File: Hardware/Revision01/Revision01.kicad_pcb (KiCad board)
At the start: 4 copper layers, 100 x 119.8 mm, 96 parts, among them J1 Battery connector, J11 RGBW connector, J2 StrainConn, J3 StrainConn, J4 StrainConn, J5 StrainConn, J6 StrainConn, J7 StrainConn, J8 StrainConn, J9 StrainConn, Q1 PMOS, Q2 NMOS, Q3 PMOS, SW1 StartStop_Push, SW2 ON/OFF_SW_SPST_LED, U1 NCP1117LPST50T3G, U2 NUCLEO-L476RG, U3 LP5813BDRRR, U4 MRF89XAM9AT-I/RM, U5 ICM-45605

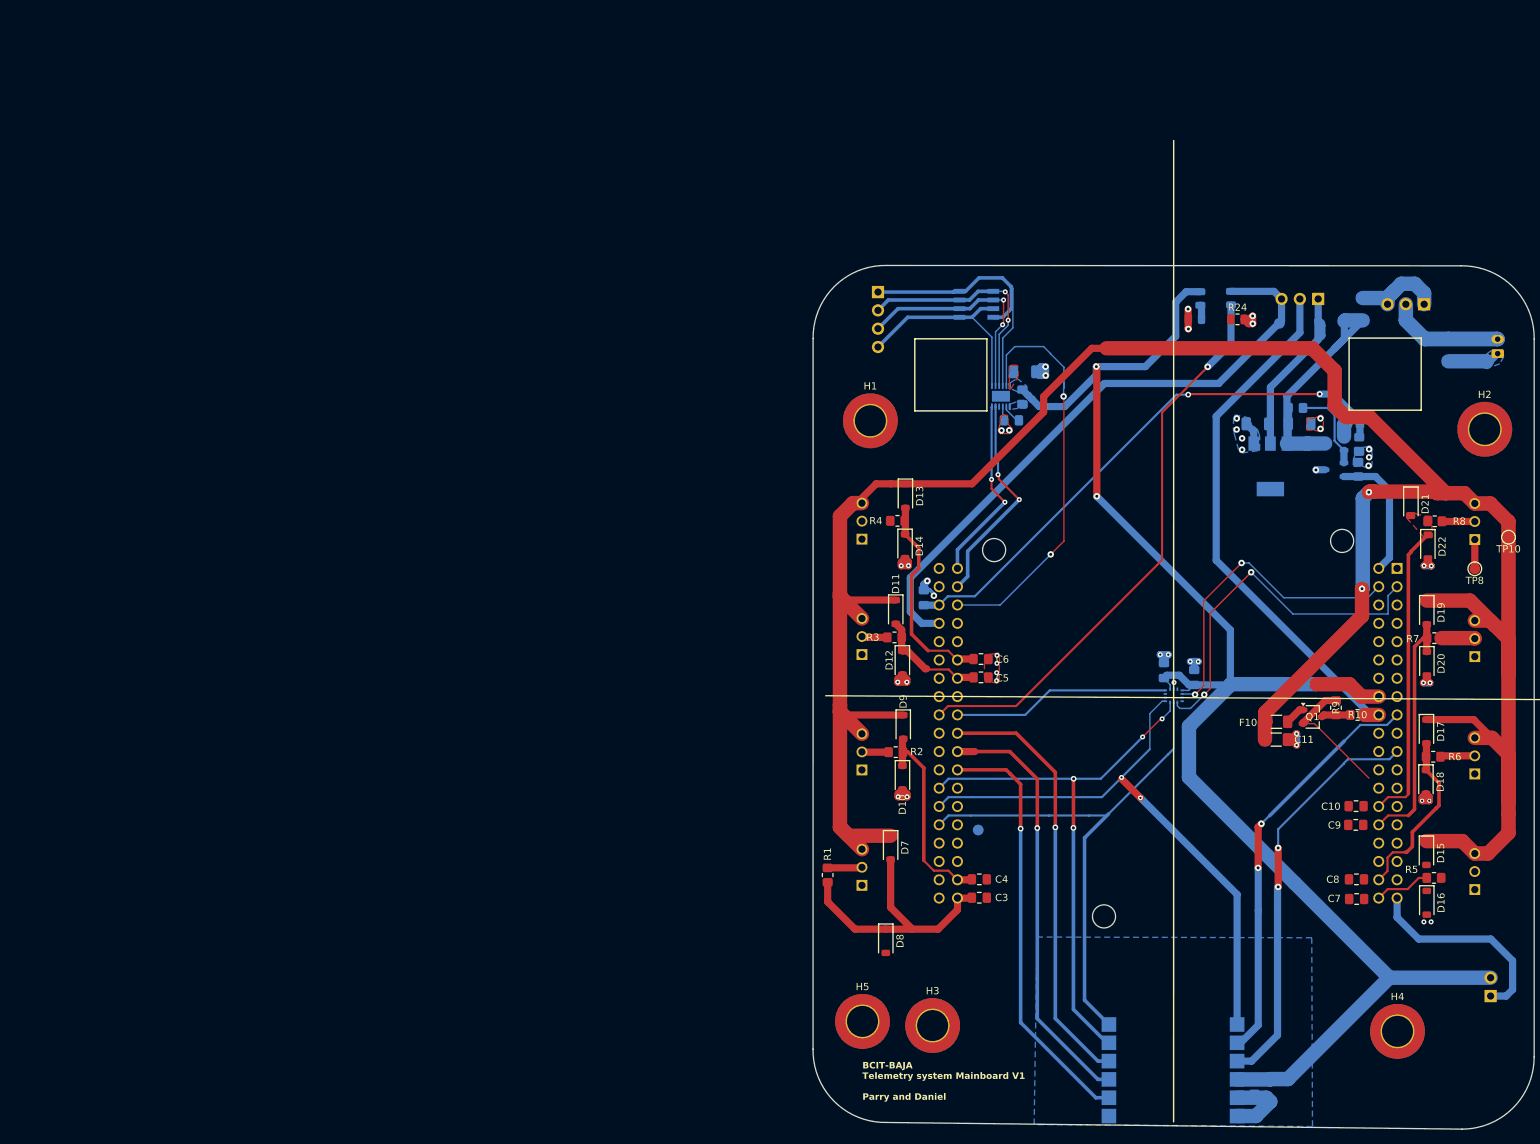
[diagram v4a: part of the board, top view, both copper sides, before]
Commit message: rewired and re-routed traces on strainAmplifier
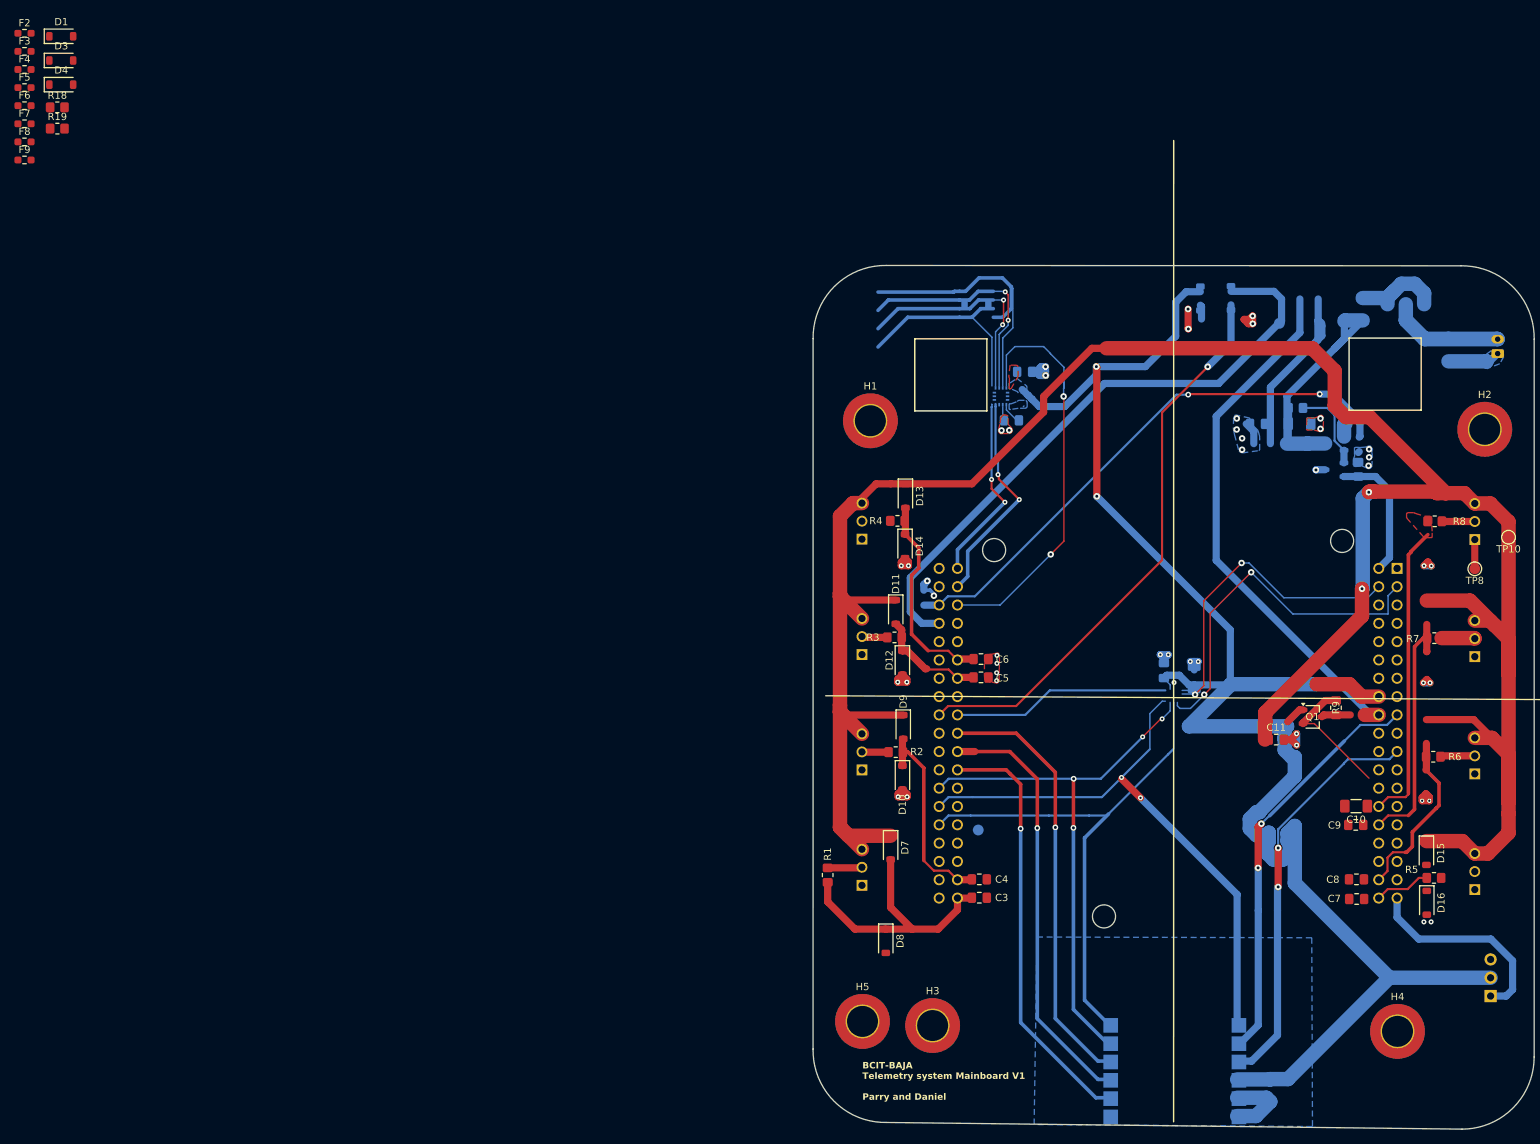
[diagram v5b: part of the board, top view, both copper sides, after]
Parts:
- removed C16, C17: 0.1uF, Capacitor_SMD:C_0805_2012Metric_Pad1.18x1.45mm_HandSolder
- removed C18, C30: 10uF, Capacitor_SMD:C_1206_3216Metric_Pad1.33x1.80mm_HandSolder
- removed D17, D18, D19, D20, D21, D22: D_Schottky_Small, Diode_SMD:D_SOD-123
- removed F10: 125mA hold, 290mA trip, Resistor_SMD:R_1206_3216Metric_Pad1.30x1.75mm_HandSolder
- removed J11: RGBW connector, Connector_PinHeader_2.54mm:PinHeader_1x04_P2.54mm_Vertical
- removed JP1: Jumper_3_Bridged12, Connector_PinHeader_2.54mm:PinHeader_1x03_P2.54mm_Vertical
- removed L1: 1uH, Inductor_SMD:L_0805_2012Metric_Pad1.15x1.40mm_HandSolder
- removed R10: 0K +-1%, Resistor_SMD:R_0805_2012Metric_Pad1.20x1.40mm_HandSolder
- removed R22: 15K +-1%, Resistor_SMD:R_0805_2012Metric_Pad1.20x1.40mm_HandSolder
- removed R23: 3.3K +-1%, Resistor_SMD:R_0805_2012Metric_Pad1.20x1.40mm_HandSolder
- removed R24, R25: 330 +-5%, Resistor_SMD:R_0805_2012Metric
- removed SW2: ON/OFF_SW_SPST_LED, Connector_PinHeader_2.54mm:PinHeader_1x03_P2.54mm_Vertical
- removed U4: MRF89XAM9AT-I/RM, MRF89XAM9AT-antenna:MOD_MRF89XAM9A_MCH
- removed U5: ICM-45605, ICM-45605-gyroscope:XDCR_ICM-45605
- added D1: D_Schottky_Small, Diode_SMD:D_SOD-123, F.Cu at (6.77, 1.18)
- added D3: D_Schottky_Small, Diode_SMD:D_SOD-123, F.Cu at (6.77, 4.53)
- added D4: D_Schottky_Small, Diode_SMD:D_SOD-123, F.Cu at (6.77, 7.88)
- added F2: Polyfuse_Small, Resistor_SMD:R_0603_1608Metric_Pad0.98x0.95mm_HandSolder, F.Cu at (1.68, 0.76)
- added F3: Polyfuse_Small, Resistor_SMD:R_0603_1608Metric_Pad0.98x0.95mm_HandSolder, F.Cu at (1.68, 3.27)
- added F4: Polyfuse_Small, Resistor_SMD:R_0603_1608Metric_Pad0.98x0.95mm_HandSolder, F.Cu at (1.68, 5.78)
- added F5: Polyfuse_Small, Resistor_SMD:R_0603_1608Metric_Pad0.98x0.95mm_HandSolder, F.Cu at (1.68, 8.29)
- added F6: Polyfuse_Small, Resistor_SMD:R_0603_1608Metric_Pad0.98x0.95mm_HandSolder, F.Cu at (1.68, 10.8)
- added F7: Polyfuse_Small, Resistor_SMD:R_0603_1608Metric_Pad0.98x0.95mm_HandSolder, F.Cu at (1.68, 13.3)
- added F8: Polyfuse_Small, Resistor_SMD:R_0603_1608Metric_Pad0.98x0.95mm_HandSolder, F.Cu at (1.68, 15.8)
- added F9: Polyfuse_Small, Resistor_SMD:R_0603_1608Metric_Pad0.98x0.95mm_HandSolder, F.Cu at (1.68, 18.3)
- added R18: 10K +-1%, Resistor_SMD:R_0805_2012Metric_Pad1.20x1.40mm_HandSolder, F.Cu at (6.22, 11.0)
- added R19: 10K +-1%, Resistor_SMD:R_0805_2012Metric_Pad1.20x1.40mm_HandSolder, F.Cu at (6.22, 14.0)
- C10: value 10nF -> 100uF; footprint Capacitor_SMD:C_0805_2012Metric_Pad1.18x1.45mm_HandSolder -> Capacitor_SMD:C_1206_3216Metric_Pad1.33x1.80mm_HandSolder
- C11: value 100uF -> 0.1uF; footprint Capacitor_SMD:C_1206_3216Metric_Pad1.33x1.80mm_HandSolder -> Capacitor_SMD:C_0805_2012Metric_Pad1.18x1.45mm_HandSolder
- C12: value 10uF -> 0.1uF; footprint Capacitor_SMD:C_1206_3216Metric_Pad1.33x1.80mm_HandSolder -> Capacitor_SMD:C_0805_2012Metric_Pad1.18x1.45mm_HandSolder
- C13: value 22uF -> 0.1uF
- C15: value 0.1uF -> 10uF; footprint Capacitor_SMD:C_0805_2012Metric_Pad1.18x1.45mm_HandSolder -> Capacitor_SMD:C_1206_3216Metric_Pad1.33x1.80mm_HandSolder
- C2: value 10uF -> 10nF; footprint Capacitor_SMD:C_1206_3216Metric_Pad1.33x1.80mm_HandSolder -> Capacitor_SMD:C_0805_2012Metric_Pad1.18x1.45mm_HandSolder
- D2: value RGBW_LED -> D_Schottky_Small; footprint RGBW:SOL120P540X160-8N -> Diode_SMD:D_SOD-123
- D5: value BLUE LED -> D_Schottky_Small; footprint LED_SMD:LED_0805_2012Metric -> Diode_SMD:D_SOD-123
- D6: value RED LED -> D_Schottky_Small; footprint LED_SMD:LED_0805_2012Metric -> Diode_SMD:D_SOD-123
- R20: value 10K +-1% -> 15K +-1%
- R21: value 10K +-1% -> 5K +-1%
- SW1: value StartStop_Push -> ON/OFF_SW_SPST_LED; footprint Connector_PinHeader_2.54mm:PinHeader_1x02_P2.54mm_Vertical -> Connector_PinHeader_2.54mm:PinHeader_1x03_P2.54mm_Vertical
- U1: value NCP1117LPST50T3G -> NUCLEO-L476RG; footprint NCP1117LPST50T3G:SOT230P700X180-4N -> NUCLEO-L476RG:MODULE_NUCLEO-L476RG
- U2: value NUCLEO-L476RG -> MRF89XAM9AT-I/RM; footprint NUCLEO-L476RG:MODULE_NUCLEO-L476RG -> MRF89XAM9AT-antenna:MOD_MRF89XAM9A_MCH
- U3: value LP5813BDRRR -> ICM-45605; footprint Package_SON:WSON-12-1EP_3x3mm_P0.5mm_EP1.5x2.5mm -> ICM-45605-gyroscope:XDCR_ICM-45605
- moved U2 66.3 mm to (161.2, 150.8), turned to 0 degrees
- moved U1 27.6 mm to (160.3, 84.5), turned to 180 degrees
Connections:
- C1 pad 1: +V_batt -> Net-(J1-Pin_2)
- C10 pad 1: /AIN1_6 -> /Application/+StrainV
- C11 pad 1: /Application/+StrainV -> +3.3V
- C13 pad 1: Net-(U3-VOUT) -> /PC5_AIN2_14_BATT_V
- C2 pad 1: +5V_External_LDO -> /AIN1_8
- C3 pad 1: /AIN1_8 -> /AIN1_7
- C4 pad 1: /AIN1_7 -> /AIN1_11
- C5 pad 1: /AIN1_11 -> /AIN1_10
- C6 pad 1: /AIN1_10 -> /AIN1_1
- C7 pad 1: /AIN1_1 -> /AIN1_2
- C8 pad 1: /AIN1_2 -> /AIN1_5
- C9 pad 1: /AIN1_5 -> /AIN1_6
- D10 pad 1: /AIN1_7 -> /AIN1_1
- D11 pad 1: /Application/+StrainV -> +3.3V
- D11 pad 2: /AIN1_11 -> /AIN1_2
- D12 pad 1: /AIN1_11 -> /AIN1_2
- D13 pad 1: /Application/+StrainV -> +3.3V
- D13 pad 2: /AIN1_10 -> /AIN1_5
- D14 pad 1: /AIN1_10 -> /AIN1_5
- D15 pad 1: /Application/+StrainV -> +3.3V
- D15 pad 2: /AIN1_1 -> /AIN1_6
- D16 pad 1: /AIN1_1 -> /AIN1_6
- D2 pad 1: /Application/U1_OUT1 -> /AIN1_8
- D2 pad 2: /Application/U1_OUT2 -> GND
- D5 pad 1: /USB_5V_GPIO_EN -> +3.3V
- D5 pad 2: +5V_USB -> /AIN1_11
- D6 pad 1: Net-(D6-K) -> /AIN1_11
- D6 pad 2: +3.3V -> GND
- D7 pad 1: /Application/+StrainV -> +3.3V
- D7 pad 2: /AIN1_8 -> /AIN1_10
- D8 pad 1: /AIN1_8 -> /AIN1_10
- D9 pad 1: /Application/+StrainV -> +3.3V
- D9 pad 2: /AIN1_7 -> /AIN1_1
- F1 pad 2: Net-(SW2-K) -> Net-(SW1-K)
- Q1 pad 1: Net-(Q1-D) -> /Application/+StrainV
- Q1 pad 3: unconnected-(Q1-S-Pad3) -> +5V
- R20 pad 1: GND -> /PC5_AIN2_14_BATT_V
- R20 pad 2: /BatteryV_Div_Enable_GPIO -> Net-(Q3-D)
- R21 pad 1: Net-(Q2-D) -> GND
- R21 pad 2: +V_batt -> /PC5_AIN2_14_BATT_V
- R9 pad 2: unconnected-(Q1-S-Pad3) -> +5V
- SW1 pad 1: /STARTSTOP_GPIO -> Net-(SW1-K)
- SW1 pad 2: +3.3V -> Net-(J1-Pin_2)
- TP5 pad 1: Net-(U2A-BOOT0) -> Net-(U1A-BOOT0)
- U3 pad 1: Net-(U3-SW) -> /PB14_SPI2_MISO
- U3 pad 10: /Application/U1_OUT0 -> unconnected-(U3-RESV_10-Pad10)
- U3 pad 11: /LP5813_EN_GPIO -> unconnected-(U3-RESV_11-Pad11)
- U3 pad 12: +3.3V -> /ICM_CS_GPIO
- U3 pad 13: GND -> /PB13_SPI2_SCK
- U3 pad 2: Net-(U3-VOUT) -> unconnected-(U3-RESV/MAS_DA-Pad2)
- U3 pad 3: GND -> unconnected-(U3-RESV/MAS_CLK-Pad3)
- U3 pad 4: unconnected-(U3-SYNC-Pad4) -> /ICM_INT1_GPIO
- U3 pad 5: /I2C_SCL -> +3.3V
- U3 pad 6: /I2C_SDA -> GND
- U3 pad 7: /Application/U1_OUT3 -> unconnected-(U3-RESV_7-Pad7)
- U3 pad 8: /Application/U1_OUT2 -> +3.3V
- U3 pad 9: /Application/U1_OUT1 -> /ICM_INT2_GPIO
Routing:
- net +3.3V: track 218.3 -> 323.4 mm, vias 2 -> 3
- net (no net): track 0.30 -> 95.9 mm, vias 0 -> 4
- net /USB_5V_GPIO_EN: track 79.2 -> 0.00 mm, vias 1 -> 0
- net unconnected-(U3-RESV_11-Pad11): track 0.00 -> 57.3 mm, vias 0 -> 2
- net /LP5813_EN_GPIO: track 57.3 -> 0.00 mm, vias 2 -> 0
- net Net-(SW1-K): track 0.00 -> 42.2 mm
- net unconnected-(U3-RESV_10-Pad10): track 0.00 -> 40.2 mm
- net /Application/U1_OUT0: track 40.2 -> 0.00 mm
- net /Application/U1_OUT1: track 32.5 -> 0.00 mm, vias 2 -> 0
- net /Application/U1_OUT2: track 31.4 -> 0.00 mm, vias 2 -> 0
- net /I2C_SCL: track 30.2 -> 0.00 mm, vias 2 -> 0
- net /ICM_INT1_GPIO: track 30.2 -> 60.4 mm, vias 0 -> 2
- net /Application/U1_OUT3: track 28.9 -> 0.00 mm
- net /STARTSTOP_GPIO: track 28.6 -> 0.00 mm
- net unconnected-(U1B-PC9-PadCN10_1): track 0.00 -> 26.3 mm, vias 0 -> 2
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- added copper zone on B.Cu, net /PB14_SPI2_MISO
- removed copper zone on B.Cu, net Net-(U3-SW)

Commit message: Small details on PART B, restarting component placement on PART A
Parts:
- removed H5: MountingHole_Pad_MP, MountingHole:MountingHole_4.3mm_M4_ISO7380_Pad_TopBottom
- removed R18, R19: 10K +-1%, Resistor_SMD:R_0805_2012Metric_Pad1.20x1.40mm_HandSolder
- removed R20: 15K +-1%, Resistor_SMD:R_0805_2012Metric_Pad1.20x1.40mm_HandSolder
- removed R21: 5K +-1%, Resistor_SMD:R_0805_2012Metric_Pad1.20x1.40mm_HandSolder
- removed U3: ICM-45605, ICM-45605-gyroscope:XDCR_ICM-45605
- added J10: StrainConn, JST_3PIN:JST_B3B-XH-A, B.Cu at (118.9, 113.1)
- added J12: Conn_01x02, Connector_PinHeader_2.54mm:PinHeader_1x02_P2.54mm_Vertical, F.Cu at (10.4, 28.6)
- added J13: Conn_01x02, Connector_PinHeader_2.54mm:PinHeader_1x02_P2.54mm_Vertical, F.Cu at (15.1, 28.6)
- added R10: 1M +-1%, Resistor_SMD:R_0805_2012Metric_Pad1.20x1.40mm_HandSolder, F.Cu at (32.6, 74.8)
- added R11: 1.6K +-1%, Resistor_SMD:R_0805_2012Metric_Pad1.20x1.40mm_HandSolder, F.Cu at (32.6, 77.8)
- added R12: 1M +-1%, Resistor_SMD:R_0805_2012Metric_Pad1.20x1.40mm_HandSolder, F.Cu at (32.6, 80.7)
- added R13: 1.6K +-1%, Resistor_SMD:R_0805_2012Metric_Pad1.20x1.40mm_HandSolder, F.Cu at (37.3, 68.9)
- added R14: 1M +-1%, Resistor_SMD:R_0805_2012Metric_Pad1.20x1.40mm_HandSolder, F.Cu at (37.3, 71.9)
- added R15: 1.6K +-1%, Resistor_SMD:R_0805_2012Metric_Pad1.20x1.40mm_HandSolder, F.Cu at (37.3, 74.8)
- added R16: 1M +-1%, Resistor_SMD:R_0805_2012Metric_Pad1.20x1.40mm_HandSolder, F.Cu at (37.3, 77.8)
- added R17: 10K +-1%, Resistor_SMD:R_0805_2012Metric_Pad1.20x1.40mm_HandSolder, F.Cu at (6.62, 9.82)
- added R26: 10K +-1%, Resistor_SMD:R_0805_2012Metric_Pad1.20x1.40mm_HandSolder, F.Cu at (11.4, 0.97)
- added R27: 10K +-1%, Resistor_SMD:R_0805_2012Metric_Pad1.20x1.40mm_HandSolder, F.Cu at (11.4, 3.92)
- added R28: 15K +-1%, Resistor_SMD:R_0805_2012Metric_Pad1.20x1.40mm_HandSolder, F.Cu at (11.4, 6.88)
- added R29: 5K +-1%, Resistor_SMD:R_0805_2012Metric_Pad1.20x1.40mm_HandSolder, F.Cu at (11.4, 9.82)
- C12, C13, C14, C15, Q2, Q3, TP1, TP2, TP3, TP4: moved to F.Cu
- J1: value Battery connector -> CANBUS backup; footprint Connector_JST:JST_PH_B2B-PH-K_1x02_P2.00mm_Vertical -> Connector_PinHeader_2.54mm:PinHeader_1x04_P2.54mm_Vertical; moved to F.Cu
- J2: value StrainConn -> Battery connector; footprint JST:JST_B3B-XH-A -> Connector_JST:JST_PH_B2B-PH-K_1x02_P2.00mm_Vertical
- J3, J4, J5, J6, J7, J8, J9: footprint JST:JST_B3B-XH-A -> JST_3PIN:JST_B3B-XH-A
- R2, R4, R6, R8: value 1.6K +-1% -> 1M +-1%
- R9: value 10K +-1% -> 1.6K +-1%
- moved FID1 230.4 mm to (43.1, 2.93)
- moved FID2 230.4 mm to (43.1, 6.48)
- moved FID3 229.2 mm to (43.1, 10.0)
- moved TP5 228.3 mm to (46.7, 10.0)
- moved TP6 227.2 mm to (46.7, 13.6)
- moved TP7 227.2 mm to (46.7, 17.1)
- moved TP9 220.1 mm to (66.0, 6.48)
- moved J1 200.9 mm to (5.78, 28.6), turned to 0 degrees
- moved R5 174.0 mm to (27.8, 77.8)
- moved C7 172.1 mm to (23.1, 66.6)
- moved R6 170.4 mm to (27.8, 80.7)
- moved C8 170.4 mm to (23.1, 69.6)
- moved D15 169.7 mm to (33.8, 64.6)
- moved D16 168.8 mm to (37.2, 64.6)
- moved C9 167.6 mm to (23.1, 72.7)
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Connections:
- C1 pad 1: Net-(J1-Pin_2) -> Net-(J2-Pin_2)
- F1 pad 2: Net-(SW1-K) -> Net-(SW1-A)
- J1 pad 1: GND -> /PB13_SPI2_SCK
- J1 pad 2: Net-(J1-Pin_2) -> /PB14_SPI2_MISO
- J2 pad 2: /Application/OpAmpOutput1 -> Net-(J2-Pin_2)
- J3 pad 2: /Application/OpAmpOutput2 -> /Application/OpAmpOutput1
- J4 pad 2: /Application/OpAmpOutput3 -> /Application/OpAmpOutput2
- J5 pad 2: /Application/OpAmpOutput4 -> /Application/OpAmpOutput3
- J6 pad 2: /Application/OpAmpOutput5 -> /Application/OpAmpOutput4
- J7 pad 2: /Application/OpAmpOutput6 -> /Application/OpAmpOutput5
- J8 pad 2: /Application/OpAmpOutput7 -> /Application/OpAmpOutput6
- J9 pad 2: /Application/OpAmpOutput8 -> /Application/OpAmpOutput7
- R2 pad 1: /Application/OpAmpOutput2 -> /AIN1_8
- R2 pad 2: /AIN1_7 -> GND
- R3 pad 1: /Application/OpAmpOutput3 -> /Application/OpAmpOutput2
- R3 pad 2: /AIN1_11 -> /AIN1_7
- R4 pad 1: /Application/OpAmpOutput4 -> /AIN1_7
- R4 pad 2: /AIN1_10 -> GND
- R5 pad 1: /Application/OpAmpOutput5 -> /Application/OpAmpOutput3
- R5 pad 2: /AIN1_1 -> /AIN1_11
- R6 pad 1: /Application/OpAmpOutput6 -> /AIN1_11
- R6 pad 2: /AIN1_2 -> GND
- R7 pad 1: /Application/OpAmpOutput7 -> /Application/OpAmpOutput4
- R7 pad 2: /AIN1_5 -> /AIN1_10
- R8 pad 1: /Application/OpAmpOutput8 -> /AIN1_10
- R8 pad 2: /AIN1_6 -> GND
- R9 pad 1: /StrainV_Enable_GPIO -> /Application/OpAmpOutput5
- R9 pad 2: +5V -> /AIN1_1
- SW1 pad 1: Net-(SW1-K) -> GND
- SW1 pad 2: Net-(J1-Pin_2) -> Net-(J2-Pin_2)
- SW1 pad 3: Net-(SW1-K) -> Net-(SW1-A)
- U1 pad CN10_27: unconnected-(U1B-PB4-PadCN10_27) -> /~{CANBUS_CS_GPIO}
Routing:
- net /Application/+StrainV: track 357.3 -> 0.00 mm, vias 2 -> 0
- net +3.3V: track 323.4 -> 0.00 mm, vias 3 -> 0
- net (no net): track 95.9 -> 0.00 mm, vias 4 -> 0
- net +5V_USB: track 86.1 -> 0.00 mm
- net /PB15_SPI2_MOSI: track 83.1 -> 0.00 mm, vias 4 -> 0
- net /PB14_SPI2_MISO: track 81.3 -> 0.00 mm, vias 2 -> 0
- net +5V: track 78.5 -> 0.00 mm
- net /PC5_AIN2_14_BATT_V: track 76.4 -> 0.00 mm, vias 2 -> 0
- net /PB13_SPI2_SCK: track 76.0 -> 0.00 mm
- net GND: track 73.6 -> 0.00 mm, vias 45 -> 0
- net /ANT_CSCON_GPIO: track 61.7 -> 0.00 mm, vias 1 -> 0
- net /ICM_INT1_GPIO: track 60.4 -> 0.00 mm, vias 2 -> 0
- net /ANT_IRQ0_GPIO: track 59.8 -> 0.00 mm, vias 1 -> 0
- net /ANT_RESET_ANT_GPIO: track 59.2 -> 0.00 mm, vias 1 -> 0
- net unconnected-(U3-RESV_11-Pad11): track 57.3 -> 0.00 mm, vias 2 -> 0
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- removed copper zone on B.Cu, net +3.3V
- removed copper zone on F.Cu, net +3.3V
- removed copper zone on F.Cu, net /AIN1_5
- removed copper zone on B.Cu, net /PB14_SPI2_MISO
- removed copper zone on B.Cu, net GND
- removed copper zone on F.Cu, net GND
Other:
- board size 100 x 119.8 mm -> 100 x 110.1 mm
- board text removed: "BATTERY"
- board text removed: "USB"
